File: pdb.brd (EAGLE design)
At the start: 50 x 100 mm, 50 parts, among them J1 XT60PWFEMALE, Q1 IRFR5305PBF, Q2 IRFR5305PBF, Q3 BSN20,215, Q4 BSN20,215, Q5 BSN20,215, U1 TSR_1-2433, U2 TXB0104, U4 LTC2946CMSPBF, U5 LTC2946CMSPBF, U6 LTC2946CMSPBF, U7 AT30TS74SS8M

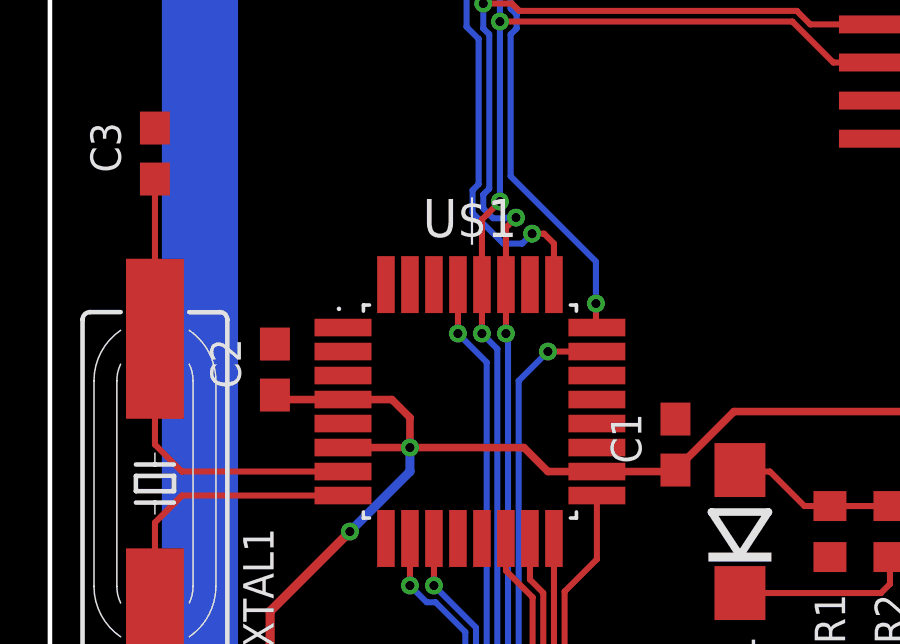
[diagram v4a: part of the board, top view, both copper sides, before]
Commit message: fixed naming, silkscreen
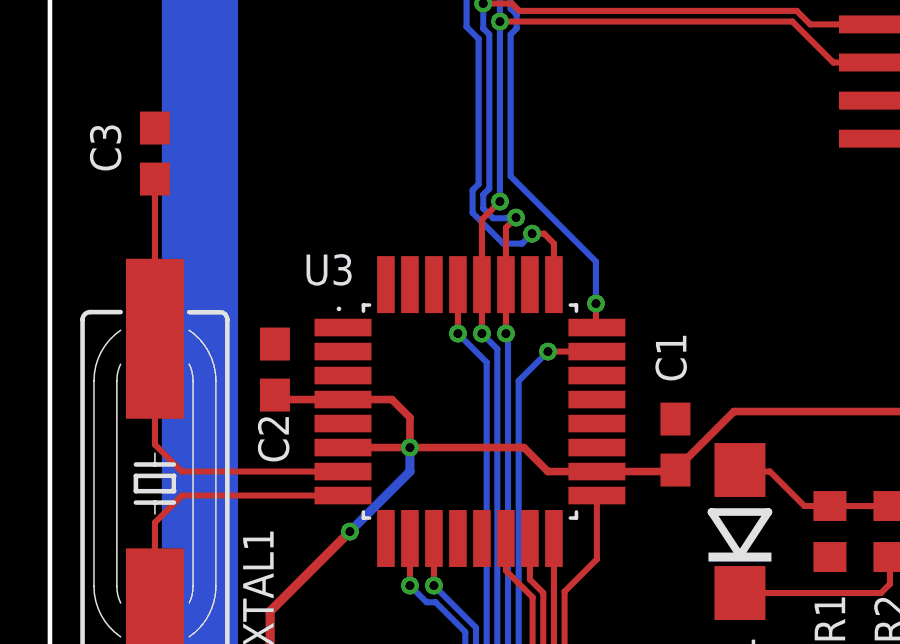
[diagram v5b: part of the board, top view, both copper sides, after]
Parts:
- renumbered U$1 to U3
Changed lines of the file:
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@@
 </element>
 <element name="C1" library="rcl" library_urn="urn:adsk.eagle:library:334" package="C0603" package3d_urn="urn:adsk.eagle:package:23616/2" value="100nF" x="20.85" y="46.9" smashed="yes" rot="R90">
-<attribute name="NAME" x="19.715" y="46.265" size="1.016" layer="25" rot="R90"/>
+<attribute name="NAME" x="21.215" y="48.965" size="1.016" layer="25" rot="R90"/>
 <attribute name="SPICEPREFIX" value="C" x="20.85" y="46.9" size="1.778" layer="27" rot="R90" display="off"/>
 <attribute name="VALUE" x="22.755" y="46.265" size="1.27" layer="27" rot="R90"/>
 </element>
 <element name="C2" library="rcl" library_urn="urn:adsk.eagle:library:334" package="C0603" package3d_urn="urn:adsk.eagle:package:23616/2" value="100nF" x="7.5" y="49.4" smashed="yes" rot="R90">
-<attribute name="NAME" x="6.365" y="48.765" size="1.016" layer="25" rot="R90"/>
+<attribute name="NAME" x="7.965" y="46.265" size="1.016" layer="25" rot="R90"/>
 <attribute name="SPICEPREFIX" value="C" x="7.5" y="49.4" size="1.778" layer="27" rot="R90" display="off"/>
 <attribute name="VALUE" x="9.405" y="48.765" size="1.27" layer="27" rot="R90"/>
@@
 <attribute name="PRICE" value="0.17 USD" x="25" y="35" size="1.778" layer="27" rot="R180" display="off"/>
 </element>
-<element name="U$1" library="jonas_atmel" library_urn="urn:adsk.eagle:library:836006" package="QFP80P900X900X120-32" package3d_urn="urn:adsk.eagle:package:2211377/1" value="ATMEGA48-20AU" x="14" y="48"/>
+<element name="U3" library="jonas_atmel" library_urn="urn:adsk.eagle:library:836006" package="QFP80P900X900X120-32" package3d_urn="urn:adsk.eagle:package:2211377/1" value="ATMEGA48-20AU" x="14" y="48" smashed="yes">
+<attribute name="NAME" x="9.3" y="52.2162" size="1.016" layer="25" align="bottom-center"/>
+<attribute name="VALUE" x="14" y="42.1838" size="1.27" layer="27" align="top-center"/>
+</element>
 </elements>
 <signals>
@@
 <contactref element="Q4" pad="2"/>
 <via x="23" y="37" extent="1-16" drill="0.3"/>
-<contactref element="U$1" pad="3"/>
-<contactref element="U$1" pad="5"/>
-<contactref element="U$1" pad="21"/>
+<contactref element="U3" pad="3"/>
+<contactref element="U3" pad="5"/>
+<contactref element="U3" pad="21"/>
 </signal>
 <signal name="V+">
@@
 <wire x1="28.2094" y1="80.25" x2="35" y2="80.25" width="0.254" layer="1"/>
 <wire x1="35" y1="80.25" x2="35" y2="74.85" width="0.254" layer="1"/>
-<contactref element="U$1" pad="18"/>
-<contactref element="U$1" pad="6"/>
-<contactref element="U$1" pad="4"/>
+<contactref element="U3" pad="18"/>
+<contactref element="U3" pad="6"/>
+<contactref element="U3" pad="4"/>
 <wire x1="9.7687" y1="46.8" x2="12" y2="46.8" width="0.254" layer="1"/>
 <wire x1="12" y1="46.8" x2="15.8" y2="46.8" width="0.254" layer="1"/>
@@
 <wire x1="26.75" y1="25.2094" x2="26.75" y2="26.2529" width="0.2032" layer="1"/>
 <wire x1="26.75" y1="26.2529" x2="25.6473" y2="27.3556" width="0.2032" layer="1"/>
-<contactref element="U$1" pad="27"/>
+<contactref element="U3" pad="27"/>
 <wire x1="15.26895" y1="50.53105" x2="15.2" y2="50.6" width="0.2032" layer="16"/>
 <via x="15.2" y="50.6" extent="1-16" drill="0.3"/>
@@
 <wire x1="26.25" y1="25.2094" x2="26.24866875" y2="25.21073125" width="0.2032" layer="1"/>
 <wire x1="26.24866875" y1="25.21073125" x2="26.24866875" y2="26.24866875" width="0.2032" layer="1"/>
-<contactref element="U$1" pad="28"/>
+<contactref element="U3" pad="28"/>
 <wire x1="14.91335" y1="50.08665" x2="14.4" y2="50.6" width="0.2032" layer="16"/>
 <via x="14.4" y="50.6" extent="1-16" drill="0.3"/>
@@
 <wire x1="27.75" y1="26.25" x2="27.5" y2="26.5" width="0.2032" layer="1"/>
 <wire x1="27.5" y1="26.5" x2="27.0058" y2="26.5" width="0.2032" layer="1"/>
-<contactref element="U$1" pad="23"/>
+<contactref element="U3" pad="23"/>
 <wire x1="17.3556" y1="35.0794" x2="17.3556" y2="37.1473" width="0.2032" layer="16"/>
 <wire x1="17.3556" y1="37.1473" x2="15.62455" y2="38.87835" width="0.2032" layer="16"/>
@@
 <wire x1="23.815409375" y1="78.75" x2="23.7906" y2="78.75" width="0.2032" layer="1"/>
 <wire x1="17.5" y1="77.25" x2="19" y2="78.75" width="0.2032" layer="16"/>
-<contactref element="U$1" pad="24"/>
+<contactref element="U3" pad="24"/>
 <wire x1="16.580675" y1="71.677775" x2="17" y2="71.677775" width="0.2032" layer="16"/>
 <wire x1="15.3556" y1="70.4527" x2="15.3556" y2="70" width="0.2032" layer="16"/>
@@
 <contactref element="U6" pad="5"/>
 <wire x1="15.25" y1="73.815409375" x2="15.25" y2="73.7906" width="0.2032" layer="1"/>
-<contactref element="U$1" pad="25"/>
+<contactref element="U3" pad="25"/>
 <via x="16.070846875" y="53.929153125" extent="1-16" drill="0.3"/>
 <wire x1="16.070846875" y1="53.929153125" x2="16.470846875" y2="53.929153125" width="0.2032" layer="1"/>
@@
 <wire x1="14.72033125" y1="33.25" x2="13.25" y2="33.25" width="0.2032" layer="16"/>
 <wire x1="15.76953125" y1="32.2008" x2="14.72033125" y2="33.25" width="0.2032" layer="16"/>
-<contactref element="U$1" pad="17"/>
+<contactref element="U3" pad="17"/>
 <wire x1="17.1556" y1="39.1556" x2="17.1556" y2="42" width="0.2032" layer="1"/>
 <wire x1="15.175" y1="37.175" x2="17.1556" y2="39.1556" width="0.2032" layer="1"/>
@@
 <wire x1="14.499" y1="15.02584375" x2="15.3944" y2="15.92124375" width="0.2032" layer="1"/>
 <wire x1="15.3944" y1="15.92124375" x2="15.3944" y2="33.7944" width="0.2032" layer="1"/>
-<contactref element="U$1" pad="29"/>
+<contactref element="U3" pad="29"/>
 <wire x1="13.6" y1="52.2313" x2="13.6" y2="50.6" width="0.2032" layer="1"/>
 <via x="13.6" y="50.6" extent="1-16" drill="0.3"/>
@@
 <wire x1="7.746" y1="32.9989" x2="7.746" y2="29.2511" width="0.2032" layer="1"/>
 <wire x1="7.746" y1="29.2511" x2="9.7" y2="27.2971" width="0.2032" layer="1"/>
-<contactref element="U$1" pad="14"/>
+<contactref element="U3" pad="14"/>
 <wire x1="15.2" y1="43.7687" x2="15.2" y2="42.6971" width="0.2032" layer="1"/>
 <wire x1="15.2" y1="42.6971" x2="16.0888" y2="41.8083" width="0.2032" layer="1"/>
@@
 <wire x1="10.75943125" y1="34.0492" x2="10.76953125" y2="34.0593" width="0.2032" layer="1"/>
 <wire x1="10.76953125" y1="34.0593" x2="11.0535" y2="34.0593" width="0.2032" layer="1"/>
-<contactref element="U$1" pad="15"/>
+<contactref element="U3" pad="15"/>
 <wire x1="11.0535" y1="34.0593" x2="16.4444" y2="39.4502" width="0.2032" layer="1"/>
 <wire x1="16.4444" y1="41.9556" x2="16" y2="42.4" width="0.2032" layer="1"/>
@@
 <wire x1="15.51523125" y1="32.958" x2="14.66683125" y2="33.8064" width="0.2032" layer="16"/>
 <wire x1="14.66683125" y1="33.8064" x2="13.01953125" y2="33.8064" width="0.2032" layer="16"/>
-<contactref element="U$1" pad="16"/>
+<contactref element="U3" pad="16"/>
 <wire x1="16.8" y1="39.3029" x2="16.8" y2="43.7687" width="0.2032" layer="1"/>
 <wire x1="11" y1="33.5029" x2="16.8" y2="39.3029" width="0.2032" layer="1"/>
@@
 <contactref element="XTAL1" pad="2"/>
 <contactref element="C3" pad="1"/>
-<contactref element="U$1" pad="7"/>
+<contactref element="U3" pad="7"/>
 <wire x1="9.7687" y1="46" x2="4.4" y2="46" width="0.2032" layer="1"/>
 <wire x1="4.4" y1="46" x2="3.5" y2="46.9" width="0.2032" layer="1"/>
@@
 <contactref element="XTAL1" pad="1"/>
 <contactref element="C4" pad="1"/>
-<contactref element="U$1" pad="8"/>
+<contactref element="U3" pad="8"/>
 <wire x1="9.7687" y1="45.2" x2="4.4" y2="45.2" width="0.2032" layer="1"/>
 <wire x1="4.4" y1="45.2" x2="3.5" y2="44.3" width="0.2032" layer="1"/>
@@
 <wire x1="19.5447875" y1="38.804" x2="21.521" y2="38.804" width="0.2032" layer="1"/>
 <wire x1="21.521" y1="38.804" x2="21.85" y2="38.475" width="0.2032" layer="1"/>
-<contactref element="U$1" pad="11"/>
+<contactref element="U3" pad="11"/>
 <wire x1="14.20215" y1="38.2702" x2="15.9332" y2="36.53915" width="0.2032" layer="16"/>
 <wire x1="14.20215" y1="40.79785" x2="12.8" y2="42.2" width="0.2032" layer="16"/>
@@
 <wire x1="19.3974875" y1="39.1596" x2="25.2929" y2="39.1596" width="0.2032" layer="1"/>
 <wire x1="25.2929" y1="39.1596" x2="25.85" y2="38.6025" width="0.2032" layer="1"/>
-<contactref element="U$1" pad="10"/>
+<contactref element="U3" pad="10"/>
 <via x="12" y="42.2" extent="1-16" drill="0.3"/>
 <via x="15.236175" y="36.44930625" extent="1-16" drill="0.3"/>
